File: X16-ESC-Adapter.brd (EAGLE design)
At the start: 101.6 x 41.1 mm, 9 parts, among them J1 BM08B-SRSS-TB(LF)(SN)

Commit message: Update X16-ESC-Adapter.brd
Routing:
- net GND: vias 0 -> 17
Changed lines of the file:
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@@
 <vertex x="59.182" y="35.052"/>
 </polygon>
+<via x="53.086" y="27.432" extent="1-16" drill="0.35"/>
+<via x="56.642" y="27.432" extent="1-16" drill="0.35"/>
+<via x="59.69" y="27.432" extent="1-16" drill="0.35"/>
+<via x="62.738" y="27.432" extent="1-16" drill="0.35"/>
+<via x="62.738" y="31.75" extent="1-16" drill="0.35"/>
+<via x="62.738" y="35.56" extent="1-16" drill="0.35"/>
+<via x="59.69" y="35.56" extent="1-16" drill="0.35"/>
+<via x="59.69" y="31.75" extent="1-16" drill="0.35"/>
+<via x="71.882" y="35.306" extent="1-16" drill="0.35"/>
+<via x="71.882" y="39.37" extent="1-16" drill="0.35"/>
+<via x="75.946" y="39.37" extent="1-16" drill="0.35"/>
+<via x="75.946" y="35.306" extent="1-16" drill="0.35"/>
+<via x="95.758" y="39.37" extent="1-16" drill="0.35"/>
+<via x="99.822" y="39.37" extent="1-16" drill="0.35"/>
+<via x="95.758" y="35.306" extent="1-16" drill="0.35"/>
+<via x="99.822" y="35.306" extent="1-16" drill="0.35"/>
 </signal>
 <signal name="GND">
@@
 </polygon>
 <wire x1="56.134" y1="38.862" x2="61.688" y2="38.862" width="0.762" layer="1"/>
+<via x="1.524" y="39.37" extent="1-16" drill="0.35"/>
+<via x="5.588" y="39.37" extent="1-16" drill="0.35"/>
+<via x="1.524" y="35.306" extent="1-16" drill="0.35"/>
+<via x="5.588" y="35.306" extent="1-16" drill="0.35"/>
+<via x="35.814" y="39.624" extent="1-16" drill="0.35"/>
+<via x="39.37" y="39.624" extent="1-16" drill="0.35"/>
+<via x="42.672" y="39.624" extent="1-16" drill="0.35"/>
+<via x="35.814" y="35.56" extent="1-16" drill="0.35"/>
+<via x="39.37" y="35.56" extent="1-16" drill="0.35"/>
+<via x="42.672" y="35.56" extent="1-16" drill="0.35"/>
+<via x="39.37" y="31.496" extent="1-16" drill="0.35"/>
+<via x="42.672" y="31.496" extent="1-16" drill="0.35"/>
+<via x="39.37" y="27.432" extent="1-16" drill="0.35"/>
+<via x="42.672" y="27.432" extent="1-16" drill="0.35"/>
+<via x="46.228" y="27.432" extent="1-16" drill="0.35"/>
+<via x="49.784" y="27.432" extent="1-16" drill="0.35"/>
+<via x="49.784" y="31.496" extent="1-16" drill="0.35"/>
 </signal>
 <signal name="ESC3A">
@@
 <wire x1="63.788" y1="38.862" x2="67.222" y2="38.862" width="0.762" layer="1"/>
 </signal>
-<signal name="N$2">
-<via x="39.37" y="27.432" extent="1-16" drill="0.35"/>
-</signal>
-<signal name="N$6">
-<via x="42.672" y="27.432" extent="1-16" drill="0.35"/>
-</signal>
-<signal name="N$10">
-<via x="46.228" y="27.432" extent="1-16" drill="0.35"/>
-</signal>
-<signal name="N$24">
-<via x="39.37" y="35.56" extent="1-16" drill="0.35"/>
-</signal>
-<signal name="N$44">
-<via x="35.814" y="39.624" extent="1-16" drill="0.35"/>
-</signal>
-<signal name="N$45">
-<via x="39.37" y="31.496" extent="1-16" drill="0.35"/>
-</signal>
-<signal name="N$49">
-<via x="42.672" y="31.496" extent="1-16" drill="0.35"/>
-</signal>
-<signal name="N$55">
-<via x="39.37" y="39.624" extent="1-16" drill="0.35"/>
-</signal>
-<signal name="N$65">
-<via x="42.672" y="39.624" extent="1-16" drill="0.35"/>
-</signal>
-<signal name="N$67">
-<via x="42.672" y="35.56" extent="1-16" drill="0.35"/>
-</signal>
-<signal name="N$3">
-<via x="59.69" y="35.56" extent="1-16" drill="0.35"/>
-</signal>
-<signal name="N$4">
-<via x="62.738" y="35.56" extent="1-16" drill="0.35"/>
-</signal>
-<signal name="N$7">
-<via x="95.758" y="35.306" extent="1-16" drill="0.35"/>
-</signal>
-<signal name="N$9">
-<via x="35.814" y="35.56" extent="1-16" drill="0.35"/>
-</signal>
-<signal name="N$12">
-<via x="95.758" y="39.37" extent="1-16" drill="0.35"/>
-</signal>
-<signal name="N$13">
-<via x="99.822" y="39.37" extent="1-16" drill="0.35"/>
-</signal>
-<signal name="N$14">
-<via x="99.822" y="35.306" extent="1-16" drill="0.35"/>
-</signal>
-<signal name="N$15">
-<via x="71.882" y="35.306" extent="1-16" drill="0.35"/>
-</signal>
-<signal name="N$16">
-<via x="75.946" y="35.306" extent="1-16" drill="0.35"/>
-</signal>
-<signal name="N$17">
-<via x="71.882" y="39.37" extent="1-16" drill="0.35"/>
-</signal>
-<signal name="N$18">
-<via x="75.946" y="39.37" extent="1-16" drill="0.35"/>
-</signal>
-<signal name="N$19">
-<via x="59.69" y="27.432" extent="1-16" drill="0.35"/>
-</signal>
-<signal name="N$20">
-<via x="62.738" y="27.432" extent="1-16" drill="0.35"/>
-</signal>
-<signal name="N$21">
-<via x="59.69" y="31.75" extent="1-16" drill="0.35"/>
-</signal>
-<signal name="N$22">
-<via x="62.738" y="31.75" extent="1-16" drill="0.35"/>
-</signal>
-<signal name="N$26">
-<via x="49.784" y="27.432" extent="1-16" drill="0.35"/>
-</signal>
-<signal name="N$27">
-<via x="49.784" y="31.496" extent="1-16" drill="0.35"/>
-</signal>
-<signal name="N$25">
-<via x="56.642" y="27.432" extent="1-16" drill="0.35"/>
-</signal>
-<signal name="N$29">
-<via x="53.086" y="27.432" extent="1-16" drill="0.35"/>
-</signal>
-<signal name="N$5">
-<via x="1.524" y="35.306" extent="1-16" drill="0.35"/>
-</signal>
-<signal name="N$8">
-<via x="1.524" y="39.37" extent="1-16" drill="0.35"/>
-</signal>
-<signal name="N$11">
-<via x="5.588" y="39.37" extent="1-16" drill="0.35"/>
-</signal>
-<signal name="N$23">
-<via x="5.588" y="35.306" extent="1-16" drill="0.35"/>
-</signal>
 </signals>

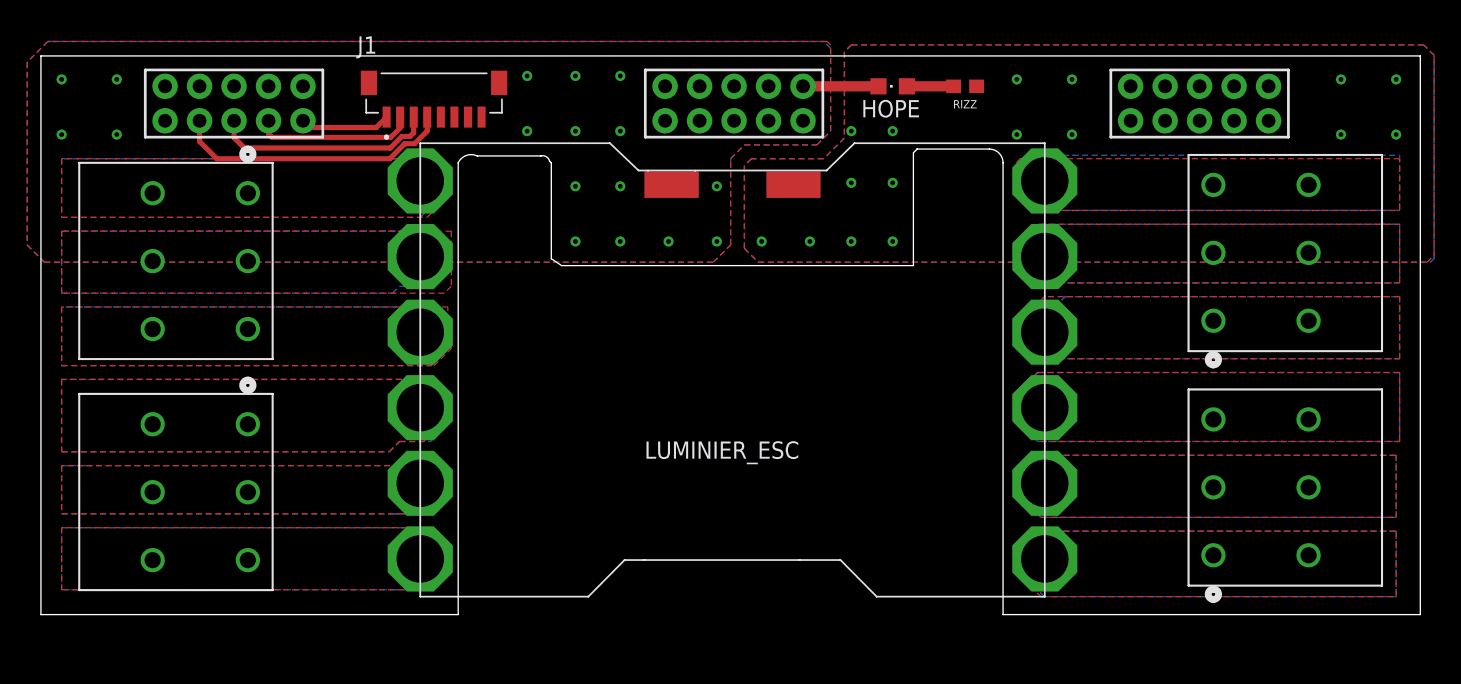
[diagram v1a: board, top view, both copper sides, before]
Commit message: Scaffolding holes updated
Scaffolding holes updated
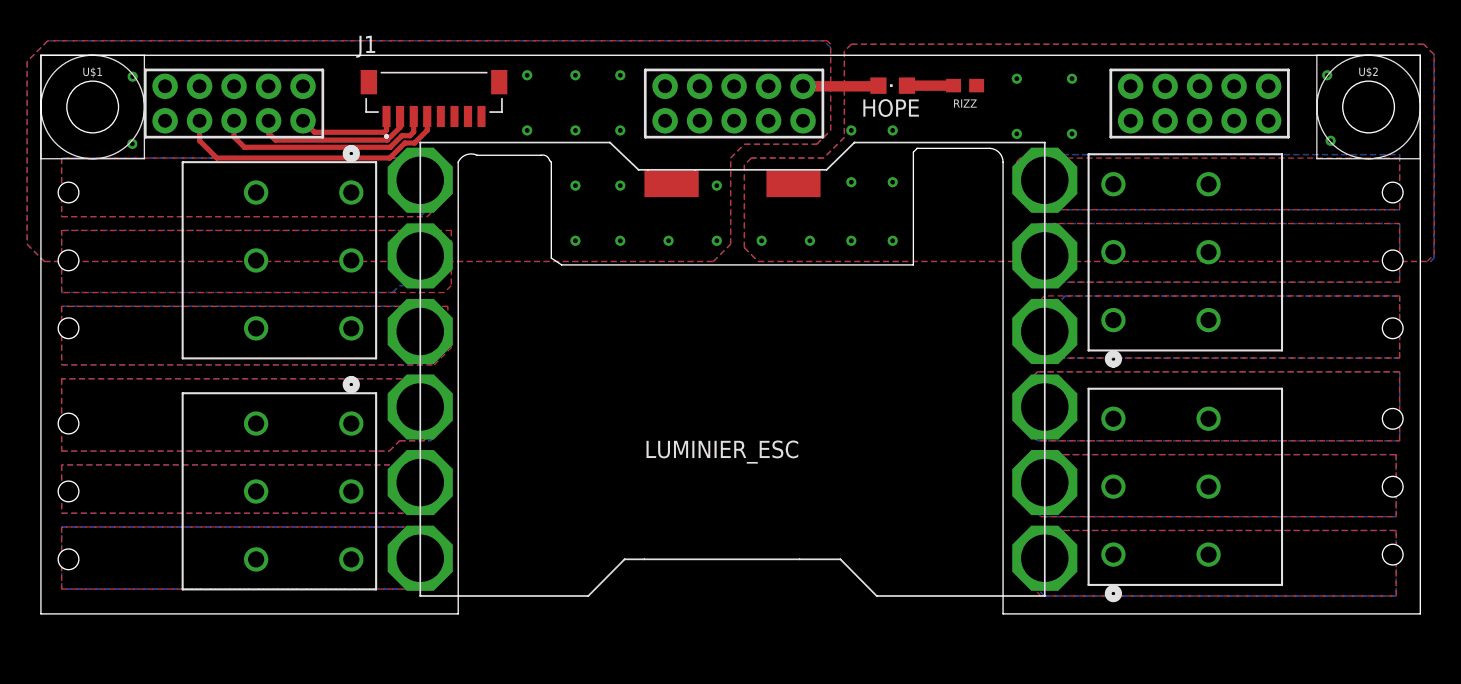
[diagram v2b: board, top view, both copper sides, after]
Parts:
- added U$1, U$2: (no value), X16-ESC-Adapter:6-32-HOLE
- moved ESC1 7.62 mm to (22.9, 31.0)
- moved ESC2 7.62 mm to (22.9, 14.0)
- moved ESC3 7.37 mm to (79.0, 4.37)
- moved ESC4 7.37 mm to (79.0, 21.6)
- moved J1 0.05 mm to (29.0, 39.2)
- moved LUMINIER_ESC 0.05 mm to (27.9, 1.32)
- moved HOPE 0.05 mm to (62.7, 38.9)
- moved RIZZ 0.05 mm to (68.1, 38.9)
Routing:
- net MTR_1: track 6.69 -> 7.58 mm
- net GND: track 5.55 -> 5.58 mm, vias 17 -> 15

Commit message: Finished!
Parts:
- PWR: device X16-ESC-Adapter:CONN_BACKPLANE_ESC_ADAPTER -> X16-NewESCAdapterConn:CONN_BACKPLANE_ESC_ADAPTER
- moved LUMINIER_ESC 0.28 mm to (27.9, 1.04)
- renumbered RIZZ to 600
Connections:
- net GND: now also J1.2, PWR.NC@1, PWR.NC@2, PWR.NC@3, PWR.NC@4, PWR.NC@5, PWR.NC@6; no longer J1.S1, J1.S2
- net MTR_1: now also J1.5; no longer J1.1
- net MTR_2: now also J1.6; no longer J1.2
- net MTR_3: now also J1.7; no longer J1.3
- net MTR_4: now also J1.8; no longer J1.4
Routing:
- net GND: track 5.58 -> 31.4 mm, vias 15 -> 12
- net MTR_3: track 16.4 -> 20.4 mm, vias 0 -> 1
- net MTR_1: track 7.58 -> 11.6 mm
- net MTR_4: track 20.6 -> 24.1 mm, vias 0 -> 1
- net MTR_2: track 12.0 -> 15.4 mm
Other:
- outline, holes or cut-outs redrawn
- board text added: "12V"
- board text added: "12V_LED"
- board text added: "C:/Users/leoja/Downloads/snoopy and woodstock.bmp"
- board text added: "C:/Users/leoja/Downloads/snoopy bmp.bmp"
- board text added: "GND"
- board text added: "R1"
- board text added: "X16 ESC Adapter Minh, Raghav, Vijay, Daniel Leo Janert"
